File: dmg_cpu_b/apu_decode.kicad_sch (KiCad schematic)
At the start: 66 parts

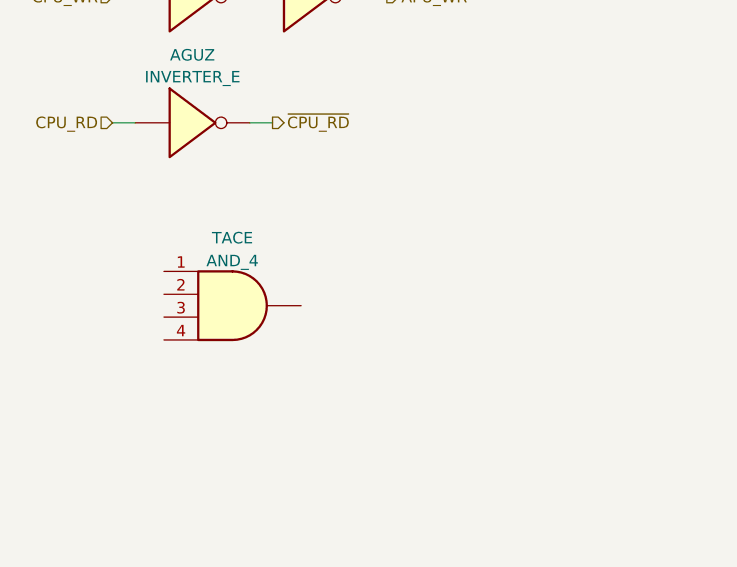
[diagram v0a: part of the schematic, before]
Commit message: CH1 Regs page completed.
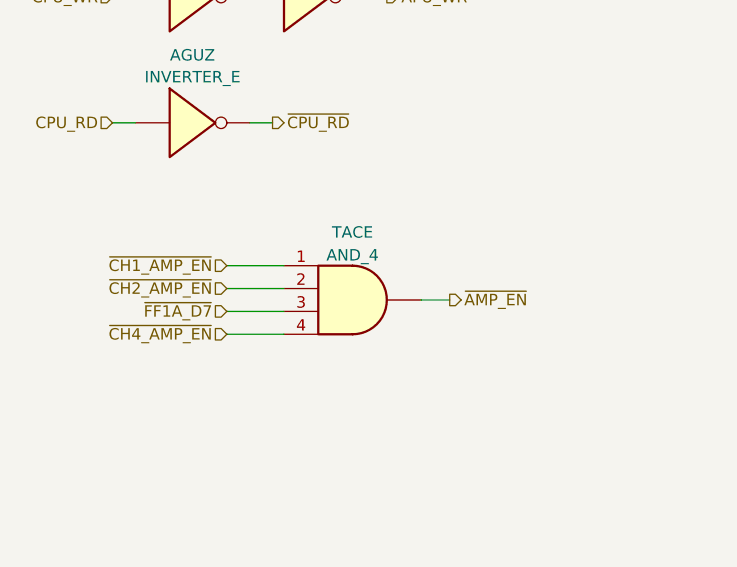
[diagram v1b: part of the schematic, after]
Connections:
- net ~{CH1_AMP_EN}: now reaches TACE.1
- net ~{CH2_AMP_EN}: now reaches TACE.2
- net ~{FF1A_D7}: now reaches TACE.3
- net ~{CH4_AMP_EN}: now reaches TACE.4
- net ~{AMP_EN}: now reaches TACE.5
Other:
- company: (none) -> CC-BY-SA-4.0 Régis Galland & Michael Singer -- Derived work from Furrtek
- title: (none) -> DMG CPU B
- moved on the sheet: TACE
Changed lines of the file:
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@@
 (kicad_sch (version 20211123) (generator eeschema)
   (paper "A3")
+  (title_block
+    (title "DMG CPU B")
+    (date "2022-03-12")
+    (rev "0")
+    (company "CC-BY-SA-4.0 Régis Galland & Michael Singer -- Derived work from Furrtek")
+    (comment 1 "https://github.com/msinger/dmg-schematics")
+  )
   (junction (at 208.28 208.915) (diameter 0) (color 0 0 0 0)
   )
@@
     (stroke (width 0) (type default) (color 0 0 0 0))
   )
+  (wire (pts (xy 69.215 208.915) (xy 75.565 208.915))
+    (stroke (width 0) (type default) (color 0 0 0 0))
+  )
   (wire (pts (xy 248.285 268.605) (xy 242.57 268.605))
     (stroke (width 0) (type default) (color 0 0 0 0))
@@
     (stroke (width 0) (type default) (color 0 0 0 0))
   )
+  (wire (pts (xy 69.215 211.455) (xy 75.565 211.455))
+    (stroke (width 0) (type default) (color 0 0 0 0))
+  )
   (wire (pts (xy 248.285 180.975) (xy 242.57 180.975))
     (stroke (width 0) (type default) (color 0 0 0 0))
@@
     (stroke (width 0) (type default) (color 0 0 0 0))
   )
+  (wire (pts (xy 69.215 213.995) (xy 75.565 213.995))
+    (stroke (width 0) (type default) (color 0 0 0 0))
+  )
   (wire (pts (xy 306.705 31.115) (xy 306.705 97.155))
     (stroke (width 0) (type default) (color 0 0 0 0))
@@
     (stroke (width 0) (type default) (color 0 0 0 0))
   )
+  (wire (pts (xy 69.215 216.535) (xy 75.565 216.535))
+    (stroke (width 0) (type default) (color 0 0 0 0))
+  )
   (wire (pts (xy 199.39 206.375) (xy 227.33 206.375))
     (stroke (width 0) (type default) (color 0 0 0 0))
@@
   )
   (wire (pts (xy 212.09 226.06) (xy 227.33 226.06))
+    (stroke (width 0) (type default) (color 0 0 0 0))
+  )
+  (wire (pts (xy 90.805 212.725) (xy 93.98 212.725))
     (stroke (width 0) (type default) (color 0 0 0 0))
   )
@@
     (effects (font (size 1.27 1.27)) (justify right))
   )
+  (hierarchical_label "~{CH2_AMP_EN}" (shape input) (at 69.215 211.455 180)
+    (effects (font (size 1.27 1.27)) (justify right))
+  )
   (hierarchical_label "CPU_RD" (shape input) (at 56.515 193.04 180)
     (effects (font (size 1.27 1.27)) (justify right))
@@
     (effects (font (size 1.27 1.27)) (justify left))
   )
+  (hierarchical_label "~{FF1A_D7}" (shape input) (at 69.215 213.995 180)
+    (effects (font (size 1.27 1.27)) (justify right))
+  )
+  (hierarchical_label "~{AMP_EN}" (shape output) (at 93.98 212.725 0)
+    (effects (font (size 1.27 1.27)) (justify left))
+  )
   (hierarchical_label "FF11" (shape output) (at 263.525 95.885 0)
     (effects (font (size 1.27 1.27)) (justify left))
@@
   (hierarchical_label "FF10" (shape output) (at 263.525 81.28 0)
     (effects (font (size 1.27 1.27)) (justify left))
+  )
+  (hierarchical_label "~{CH1_AMP_EN}" (shape input) (at 69.215 208.915 180)
+    (effects (font (size 1.27 1.27)) (justify right))
   )
   (hierarchical_label "FF20" (shape output) (at 351.79 81.28 0)
@@
   (hierarchical_label "FF1B" (shape output) (at 263.525 227.33 0)
     (effects (font (size 1.27 1.27)) (justify left))
+  )
+  (hierarchical_label "~{CH4_AMP_EN}" (shape input) (at 69.215 216.535 180)
+    (effects (font (size 1.27 1.27)) (justify right))
   )
   (hierarchical_label "FF19" (shape output) (at 263.525 198.12 0)
@@
     (pin "2")
   )
-  (symbol (lib_id "DMG_CPU_Cells:AND_4") (at 69.85 213.36 0) (unit 1)
-    (in_bom yes) (on_board yes) (fields_autoplaced)
-    (property "Reference" "TACE" (id 0) (at 69.85 205.8502 0))
-    (property "Value" "AND_4" (id 1) (at 69.85 208.3871 0))
-    (property "Footprint" "" (id 2) (at 69.85 213.36 0)
-      (effects (font (size 1.27 1.27)) hide)
-    )
-    (property "Datasheet" "http://iceboy.a-singer.de/doc/dmg_cells.html#and4" (id 3) (at 69.85 220.98 0)
-      (effects (font (size 1.27 1.27)) hide)
-    )
+  (symbol (lib_id "DMG_CPU_Cells:AND_4") (at 83.185 212.725 0) (unit 1)
+    (in_bom yes) (on_board yes) (fields_autoplaced)
+    (property "Reference" "TACE" (id 0) (at 83.185 205.2152 0))
+    (property "Value" "AND_4" (id 1) (at 83.185 207.7521 0))
+    (property "Footprint" "" (id 2) (at 83.185 212.725 0)
+      (effects (font (size 1.27 1.27)) hide)
+    )
+    (property "Datasheet" "http://iceboy.a-singer.de/doc/dmg_cells.html#and4" (id 3) (at 83.185 220.345 0)
+      (effects (font (size 1.27 1.27)) hide)
+    )

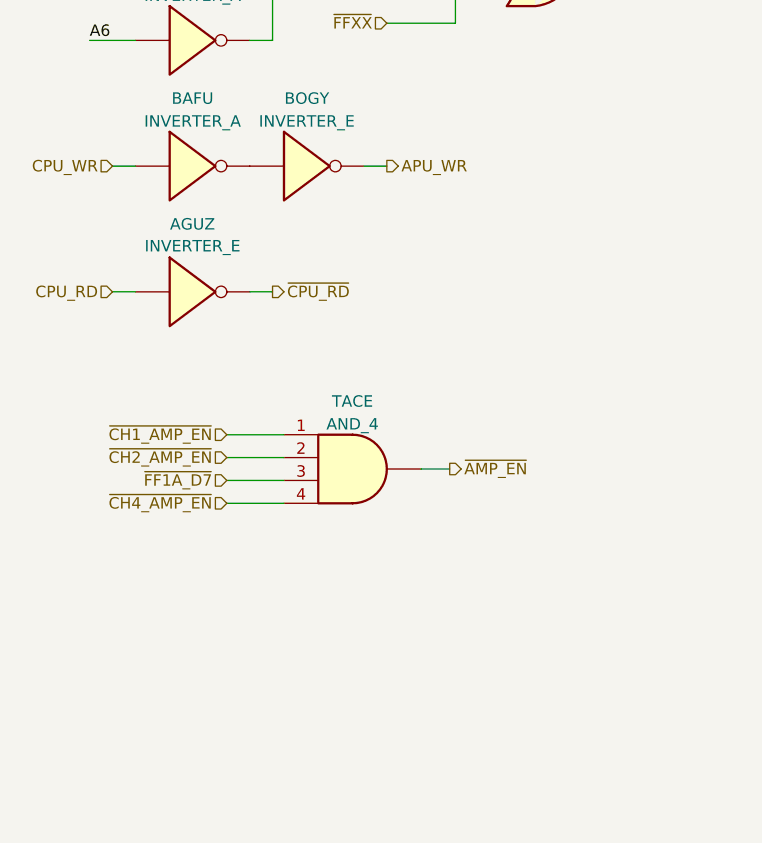
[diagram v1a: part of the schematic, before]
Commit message: CH2 Reg page added.
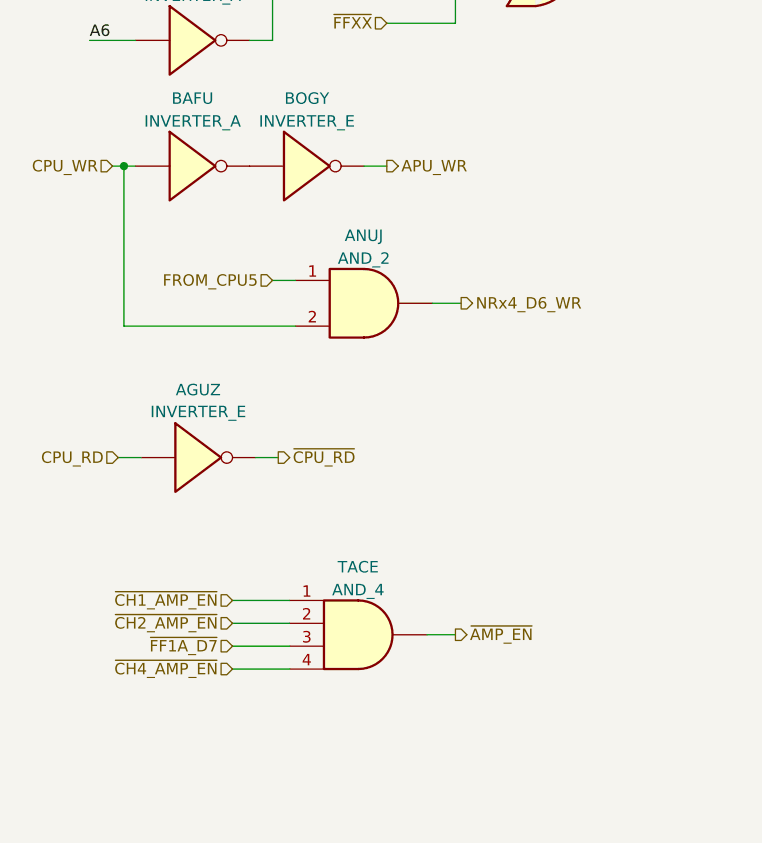
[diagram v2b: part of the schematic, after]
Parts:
- added ANUJ: AND_2, symbol DMG_CPU_Cells:AND_2
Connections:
- net CPU_WR: now also ANUJ.2
- new net FROM_CPU5: ANUJ.1
- new net NRx4_D6_WR: ANUJ.3
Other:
- moved on the sheet: AGUZ, TACE
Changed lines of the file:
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@@
   (junction (at 212.09 167.64) (diameter 0) (color 0 0 0 0)
   )
+  (junction (at 57.785 179.07) (diameter 0) (color 0 0 0 0)
+  )
   (junction (at 167.64 61.595) (diameter 0) (color 0 0 0 0)
   )
@@
     (stroke (width 0) (type default) (color 0 0 0 0))
   )
-  (wire (pts (xy 69.215 208.915) (xy 75.565 208.915))
+  (wire (pts (xy 69.85 227.33) (xy 76.2 227.33))
     (stroke (width 0) (type default) (color 0 0 0 0))
   )
@@
     (stroke (width 0) (type default) (color 0 0 0 0))
   )
+  (wire (pts (xy 57.785 196.85) (xy 76.835 196.85))
+    (stroke (width 0) (type default) (color 0 0 0 0))
+  )
+  (wire (pts (xy 74.295 191.77) (xy 76.835 191.77))
+    (stroke (width 0) (type default) (color 0 0 0 0))
+  )
   (wire (pts (xy 201.93 89.535) (xy 201.93 104.14))
     (stroke (width 0) (type default) (color 0 0 0 0))
@@
     (stroke (width 0) (type default) (color 0 0 0 0))
   )
+  (wire (pts (xy 57.785 179.07) (xy 59.055 179.07))
+    (stroke (width 0) (type default) (color 0 0 0 0))
+  )
   (wire (pts (xy 302.895 80.01) (xy 315.595 80.01))
     (stroke (width 0) (type default) (color 0 0 0 0))
@@
     (stroke (width 0) (type default) (color 0 0 0 0))
   )
+  (wire (pts (xy 92.075 194.31) (xy 95.25 194.31))
+    (stroke (width 0) (type default) (color 0 0 0 0))
+  )
   (wire (pts (xy 296.545 106.68) (xy 296.545 121.285))
     (stroke (width 0) (type default) (color 0 0 0 0))
@@
     (stroke (width 0) (type default) (color 0 0 0 0))
   )
-  (wire (pts (xy 56.515 193.04) (xy 59.055 193.04))
+  (wire (pts (xy 57.15 211.455) (xy 59.69 211.455))
     (stroke (width 0) (type default) (color 0 0 0 0))
   )
@@
     (stroke (width 0) (type default) (color 0 0 0 0))
   )
+  (wire (pts (xy 57.785 179.07) (xy 57.785 196.85))
+    (stroke (width 0) (type default) (color 0 0 0 0))
+  )
   (wire (pts (xy 76.2 139.065) (xy 81.28 139.065))
     (stroke (width 0) (type default) (color 0 0 0 0))
@@
     (stroke (width 0) (type default) (color 0 0 0 0))
   )
-  (wire (pts (xy 69.215 211.455) (xy 75.565 211.455))
+  (wire (pts (xy 69.85 229.87) (xy 76.2 229.87))
     (stroke (width 0) (type default) (color 0 0 0 0))
   )
@@
     (stroke (width 0) (type default) (color 0 0 0 0))
   )
-  (wire (pts (xy 69.215 213.995) (xy 75.565 213.995))
+  (wire (pts (xy 69.85 232.41) (xy 76.2 232.41))
     (stroke (width 0) (type default) (color 0 0 0 0))
   )
@@
     (stroke (width 0) (type default) (color 0 0 0 0))
   )
-  (wire (pts (xy 74.295 193.04) (xy 71.755 193.04))
+  (wire (pts (xy 74.93 211.455) (xy 72.39 211.455))
     (stroke (width 0) (type default) (color 0 0 0 0))
   )
@@
     (stroke (width 0) (type default) (color 0 0 0 0))
   )
-  (wire (pts (xy 56.515 179.07) (xy 59.055 179.07))
+  (wire (pts (xy 56.515 179.07) (xy 57.785 179.07))
     (stroke (width 0) (type default) (color 0 0 0 0))
   )
@@
     (stroke (width 0) (type default) (color 0 0 0 0))
   )
-  (wire (pts (xy 69.215 216.535) (xy 75.565 216.535))
+  (wire (pts (xy 69.85 234.95) (xy 76.2 234.95))
     (stroke (width 0) (type default) (color 0 0 0 0))
   )
@@
     (stroke (width 0) (type default) (color 0 0 0 0))
   )
-  (wire (pts (xy 90.805 212.725) (xy 93.98 212.725))
+  (wire (pts (xy 91.44 231.14) (xy 94.615 231.14))
     (stroke (width 0) (type default) (color 0 0 0 0))
   )
@@
     (effects (font (size 1.27 1.27)) (justify right))
   )
-  (hierarchical_label "~{CH2_AMP_EN}" (shape input) (at 69.215 211.455 180)
+  (hierarchical_label "~{CH2_AMP_EN}" (shape input) (at 69.85 229.87 180)
     (effects (font (size 1.27 1.27)) (justify right))
   )
-  (hierarchical_label "CPU_RD" (shape input) (at 56.515 193.04 180)
+  (hierarchical_label "CPU_RD" (shape input) (at 57.15 211.455 180)
     (effects (font (size 1.27 1.27)) (justify right))
   )
@@
     (effects (font (size 1.27 1.27)) (justify left))
   )
-  (hierarchical_label "~{CPU_RD}" (shape output) (at 74.295 193.04 0)
+  (hierarchical_label "~{CPU_RD}" (shape output) (at 74.93 211.455 0)
     (effects (font (size 1.27 1.27)) (justify left))
   )
@@
     (effects (font (size 1.27 1.27)) (justify left))
   )
-  (hierarchical_label "~{FF1A_D7}" (shape input) (at 69.215 213.995 180)
+  (hierarchical_label "FROM_CPU5" (shape input) (at 74.295 191.77 180)
     (effects (font (size 1.27 1.27)) (justify right))
   )
-  (hierarchical_label "~{AMP_EN}" (shape output) (at 93.98 212.725 0)
+  (hierarchical_label "~{FF1A_D7}" (shape input) (at 69.85 232.41 180)
+    (effects (font (size 1.27 1.27)) (justify right))
+  )
+  (hierarchical_label "~{AMP_EN}" (shape output) (at 94.615 231.14 0)
     (effects (font (size 1.27 1.27)) (justify left))
   )
@@
     (effects (font (size 1.27 1.27)) (justify left))
   )
-  (hierarchical_label "~{CH1_AMP_EN}" (shape input) (at 69.215 208.915 180)
+  (hierarchical_label "~{CH1_AMP_EN}" (shape input) (at 69.85 227.33 180)
     (effects (font (size 1.27 1.27)) (justify right))
   )
@@
     (effects (font (size 1.27 1.27)) (justify left))
   )
+  (hierarchical_label "NRx4_D6_WR" (shape output) (at 95.25 194.31 0)
+    (effects (font (size 1.27 1.27)) (justify left))
+  )
   (hierarchical_label "FF16" (shape output) (at 263.525 154.305 0)
     (effects (font (size 1.27 1.27)) (justify left))
@@
     (effects (font (size 1.27 1.27)) (justify left))
   )
-  (hierarchical_label "~{CH4_AMP_EN}" (shape input) (at 69.215 216.535 180)
+  (hierarchical_label "~{CH4_AMP_EN}" (shape input) (at 69.85 234.95 180)
     (effects (font (size 1.27 1.27)) (justify right))
   )
@@
     (pin "1")
     (pin "2")
+  )
+  (symbol (lib_id "DMG_CPU_Cells:AND_2") (at 84.455 194.31 0) (unit 1)
+    (in_bom yes) (on_board yes) (fields_autoplaced)
+    (property "Reference" "ANUJ" (id 0) (at 84.455 186.8002 0))
+    (property "Value" "AND_2" (id 1) (at 84.455 189.3371 0))
+    (property "Footprint" "" (id 2) (at 84.455 194.31 0)
+      (effects (font (size 1.27 1.27)) hide)
+    )
+    (property "Datasheet" "http://iceboy.a-singer.de/doc/dmg_cells.html#and2" (id 3) (at 84.455 201.93 0)
+      (effects (font (size 1.27 1.27)) hide)
+    )
+    (pin "1")
+    (pin "2")
+    (pin "3")
   )
   (symbol (lib_id "DMG_CPU_Cells:NAND_4") (at 234.95 239.395 0) (unit 1)
@@
     (pin "3")
   )
-  (symbol (lib_id "DMG_CPU_Cells:INVERTER_E") (at 65.405 193.04 0) (unit 1)
+  (symbol (lib_id "DMG_CPU_Cells:INVERTER_E") (at 66.04 211.455 0) (unit 1)
     (in_bom yes) (on_board yes)
-    (property "Reference" "AGUZ" (id 0) (at 65.405 185.5302 0))
-    (property "Value" "INVERTER_E" (id 1) (at 65.405 187.96 0))
-    (property "Footprint" "" (id 2) (at 62.865 193.04 0)
-      (effects (font (size 1.27 1.27)) hide)
-    )
-    (property "Datasheet" "http://iceboy.a-singer.de/doc/dmg_cells.html#inv_e" (id 3) (at 66.675 200.66 0)
+    (property "Reference" "AGUZ" (id 0) (at 66.04 203.9452 0))
+    (property "Value" "INVERTER_E" (id 1) (at 66.04 206.375 0))
+    (property "Footprint" "" (id 2) (at 63.5 211.455 0)
+      (effects (font (size 1.27 1.27)) hide)
+    )
+    (property "Datasheet" "http://iceboy.a-singer.de/doc/dmg_cells.html#inv_e" (id 3) (at 67.31 219.075 0)
       (effects (font (size 1.27 1.27)) hide)
     )
@@
     (pin "2")
   )
-  (symbol (lib_id "DMG_CPU_Cells:AND_4") (at 83.185 212.725 0) (unit 1)
-    (in_bom yes) (on_board yes) (fields_autoplaced)
-    (property "Reference" "TACE" (id 0) (at 83.185 205.2152 0))
-    (property "Value" "AND_4" (id 1) (at 83.185 207.7521 0))
-    (property "Footprint" "" (id 2) (at 83.185 212.725 0)
-      (effects (font (size 1.27 1.27)) hide)
-    )
-    (property "Datasheet" "http://iceboy.a-singer.de/doc/dmg_cells.html#and4" (id 3) (at 83.185 220.345 0)
-      (effects (font (size 1.27 1.27)) hide)
-    )
+  (symbol (lib_id "DMG_CPU_Cells:AND_4") (at 83.82 231.14 0) (unit 1)
+    (in_bom yes) (on_board yes) (fields_autoplaced)
+    (property "Reference" "TACE" (id 0) (at 83.82 223.6302 0))
+    (property "Value" "AND_4" (id 1) (at 83.82 226.1671 0))
+    (property "Footprint" "" (id 2) (at 83.82 231.14 0)
+      (effects (font (size 1.27 1.27)) hide)
+    )
+    (property "Datasheet" "http://iceboy.a-singer.de/doc/dmg_cells.html#and4" (id 3) (at 83.82 238.76 0)
+      (effects (font (size 1.27 1.27)) hide)
+    )

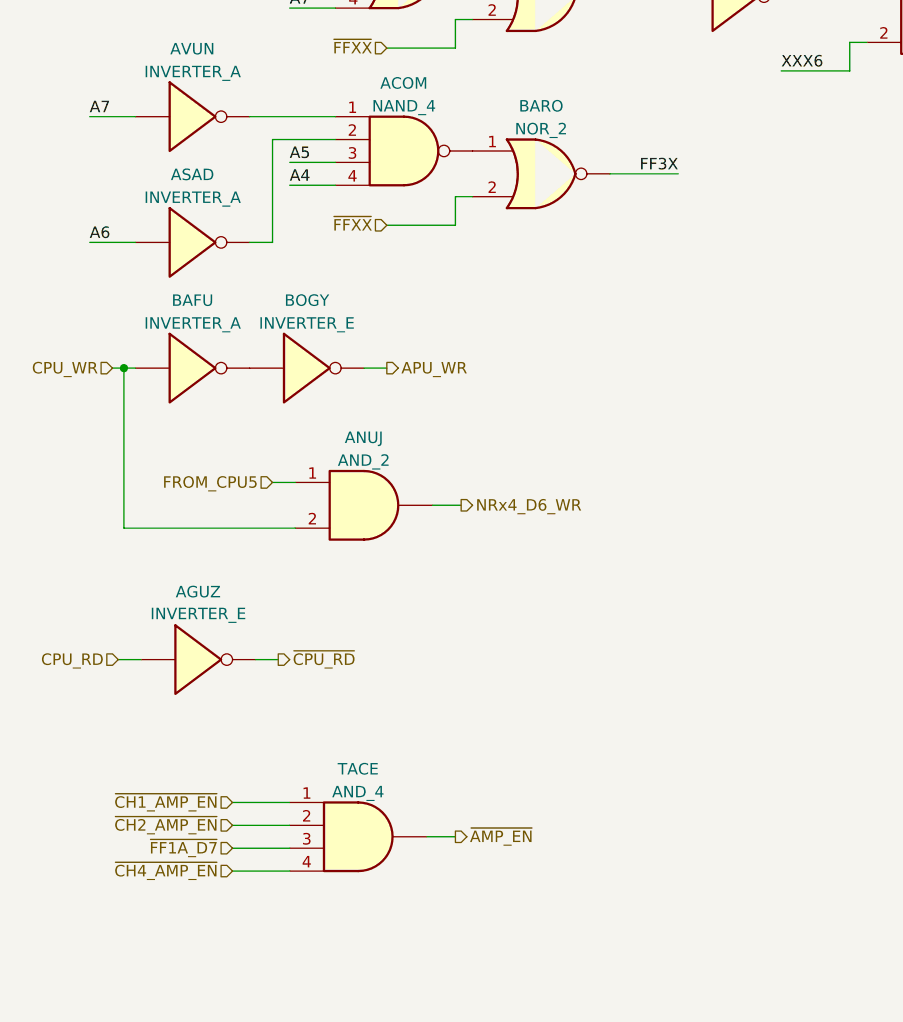
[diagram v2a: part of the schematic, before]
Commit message: Channel 2 + Channel 3 added. Channel 3 fits on 2 sheets.
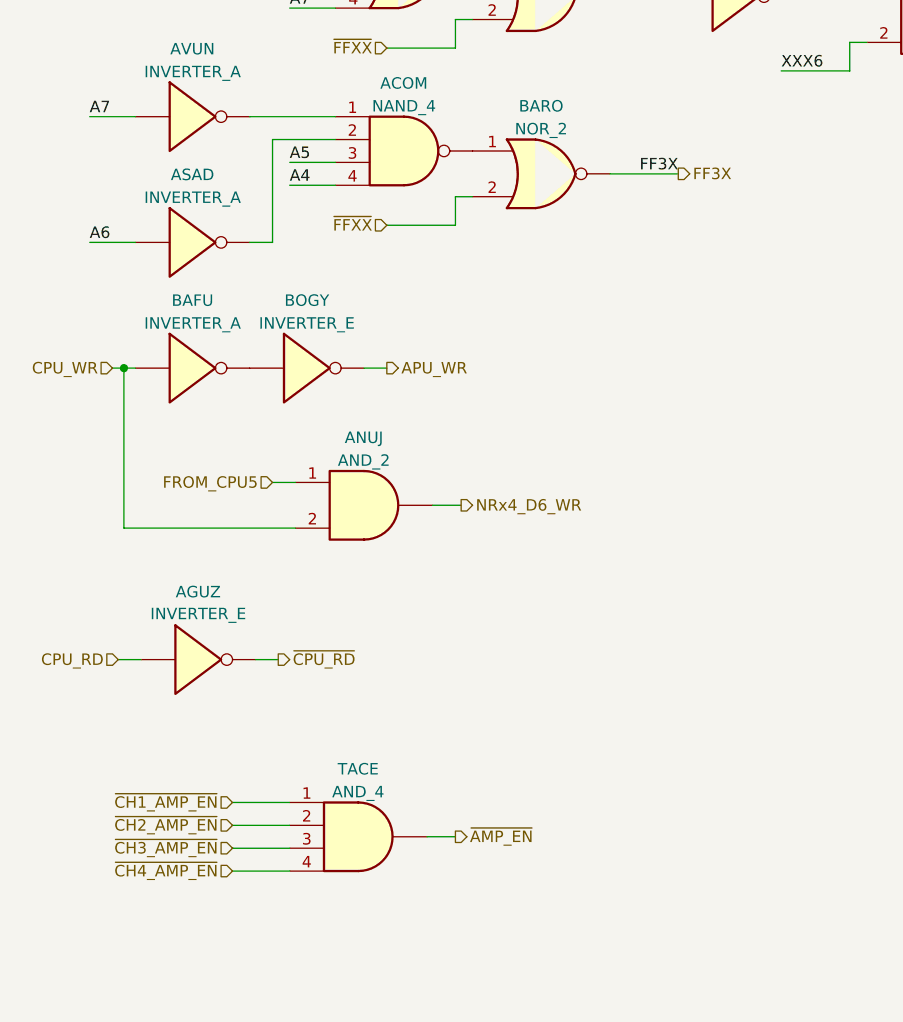
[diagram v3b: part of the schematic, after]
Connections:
- net ~{FF1A_D7} renamed ~{CH3_AMP_EN}
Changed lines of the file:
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@@
+    (effects (font (size 1.27 1.27)) (justify left))
+  )
+  (hierarchical_label "~{CH3_AMP_EN}" (shape input) (at 69.85 232.41 180)
+    (effects (font (size 1.27 1.27)) (justify right))
+  )
+  (hierarchical_label "FF3X" (shape output) (at 119.38 157.48 0)
     (effects (font (size 1.27 1.27)) (justify left))
   )
@@
     (effects (font (size 1.27 1.27)) (justify right))
   )
-  (hierarchical_label "~{FF1A_D7}" (shape input) (at 69.85 232.41 180)
-    (effects (font (size 1.27 1.27)) (justify right))
-  )
